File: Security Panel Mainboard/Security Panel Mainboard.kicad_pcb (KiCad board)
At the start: 4 copper layers, 138.7 x 99.1 mm, 66 parts, among them IC1 LM358DT, J1 CTB0508_3, J2 CTB0508_3, J3 CTB0508_3, J4 CTB0508_3, J5 CTB0508_3, J6 CTB0508_3, J7 CTB0508_5, J8 CTB0708/2, J9 SPI Programming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

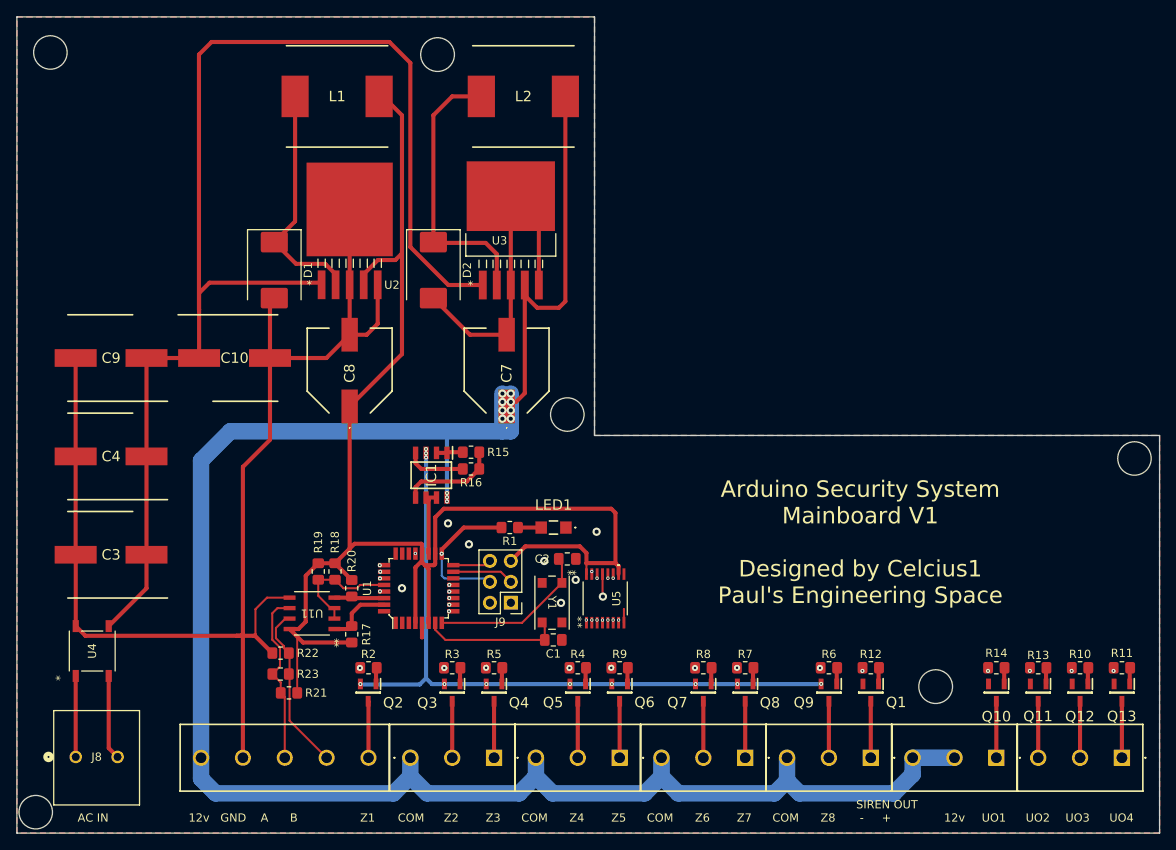
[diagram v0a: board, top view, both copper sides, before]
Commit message: Design Changes to PSU and Mainboard
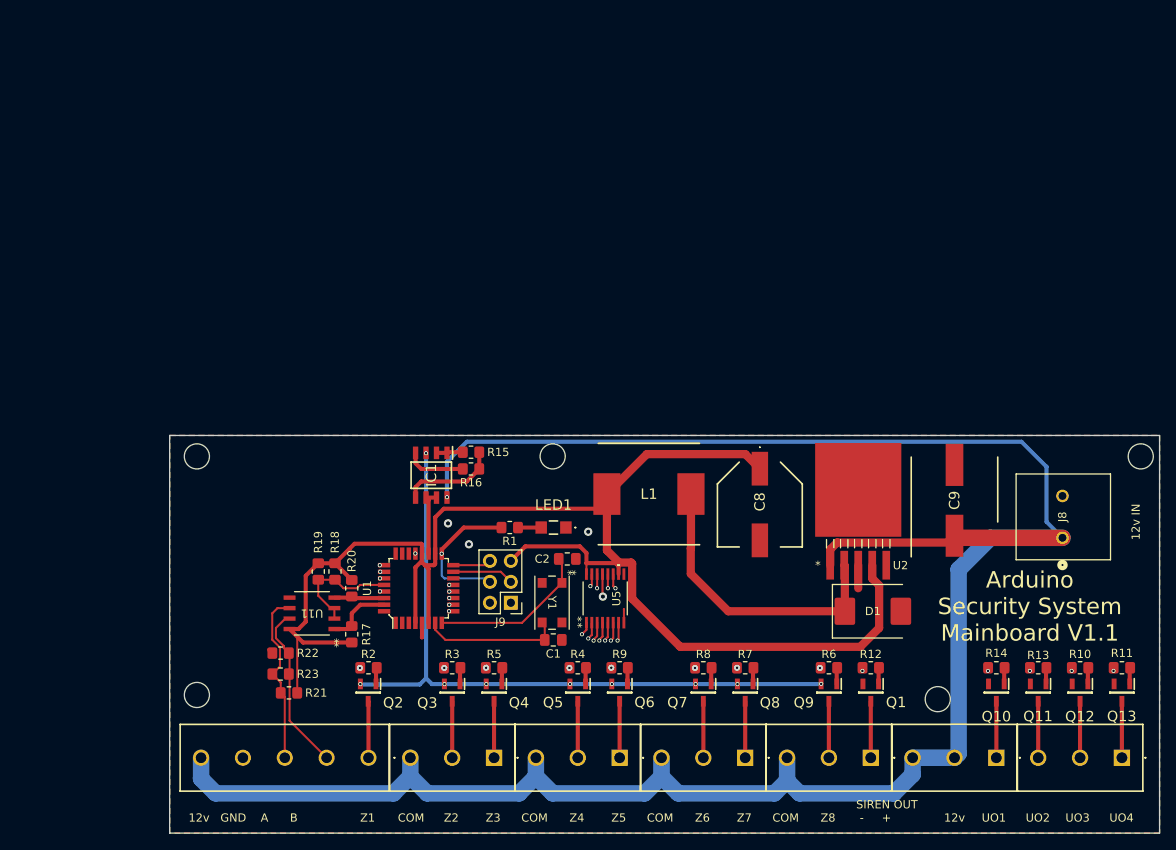
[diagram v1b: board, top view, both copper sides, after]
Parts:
- removed C10, C3, C4: 100uF, SamacSys_Parts:CAPAE1050X1250N
- removed C7: 220uF, SamacSys_Parts:EEE0JA152UAP
- removed D2: B340, Diode_SMD:D_SMC
- removed L2: MSS1210-334KED, SamacSys_Parts:INDPM123123X1020N
- removed U3: LM2576-12WU, LM2576-12WU:TO-263-5_U_MCH
- removed U4: ABS210-13, ABS210-13:SON_S210-13_DIO
- moved J8 122.7 mm to (191.4, 124.2), turned to 90 degrees
- moved C9 103.8 mm to (178.3, 119.6), turned to 90 degrees
- moved D1 83.6 mm to (168.4, 133.1), turned to 0 degrees
- moved U2 70.5 mm to (166.6, 118.4)
- moved L1 61.3 mm to (141.2, 118.9), turned to 180 degrees
- moved C8 52.4 mm to (154.7, 120.1), turned to -90 degrees
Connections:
- C9 pad 1: +24V UREG -> +12V
- J8 pad 1: +24V AC2 -> +12V
- J8 pad 2: +24V AC -> GND
- U2 pad 1: +24V UREG -> +12V
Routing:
- net GND: track 212.7 -> 16.8 mm, vias 9 -> 5
- net +24V UREG: track 155.6 -> 0.00 mm
- net Net-(D2-K): track 34.2 -> 0.00 mm
- net +12V: track 259.2 -> 270.6 mm, vias 11 -> 1
- net +24V AC: track 10.3 -> 0.00 mm
- net +24V AC2: track 9.83 -> 0.00 mm
- net Net-(D1-K): track 29.1 -> 35.9 mm
- net +5V: track 181.0 -> 185.5 mm
- net CLOCK: track 30.9 -> 34.1 mm
- net DATA: track 28.3 -> 31.3 mm
- net LATCH: track 29.1 -> 32.1 mm
- net ADC IN B: track 84.4 -> 83.9 mm, vias 11 -> 9
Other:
- board size 138.7 x 99.1 mm -> 120.1 x 48.3 mm
- board text added: "12v IN"
- board text added: "Arduino Security System Mainboard V1.1"
- board text removed: "AC IN"
- board text removed: "Arduino Security System Mainboard V1 Designed by Celcius1 Paul's Engineering Space"
